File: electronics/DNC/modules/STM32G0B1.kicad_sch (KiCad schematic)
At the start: 1 part

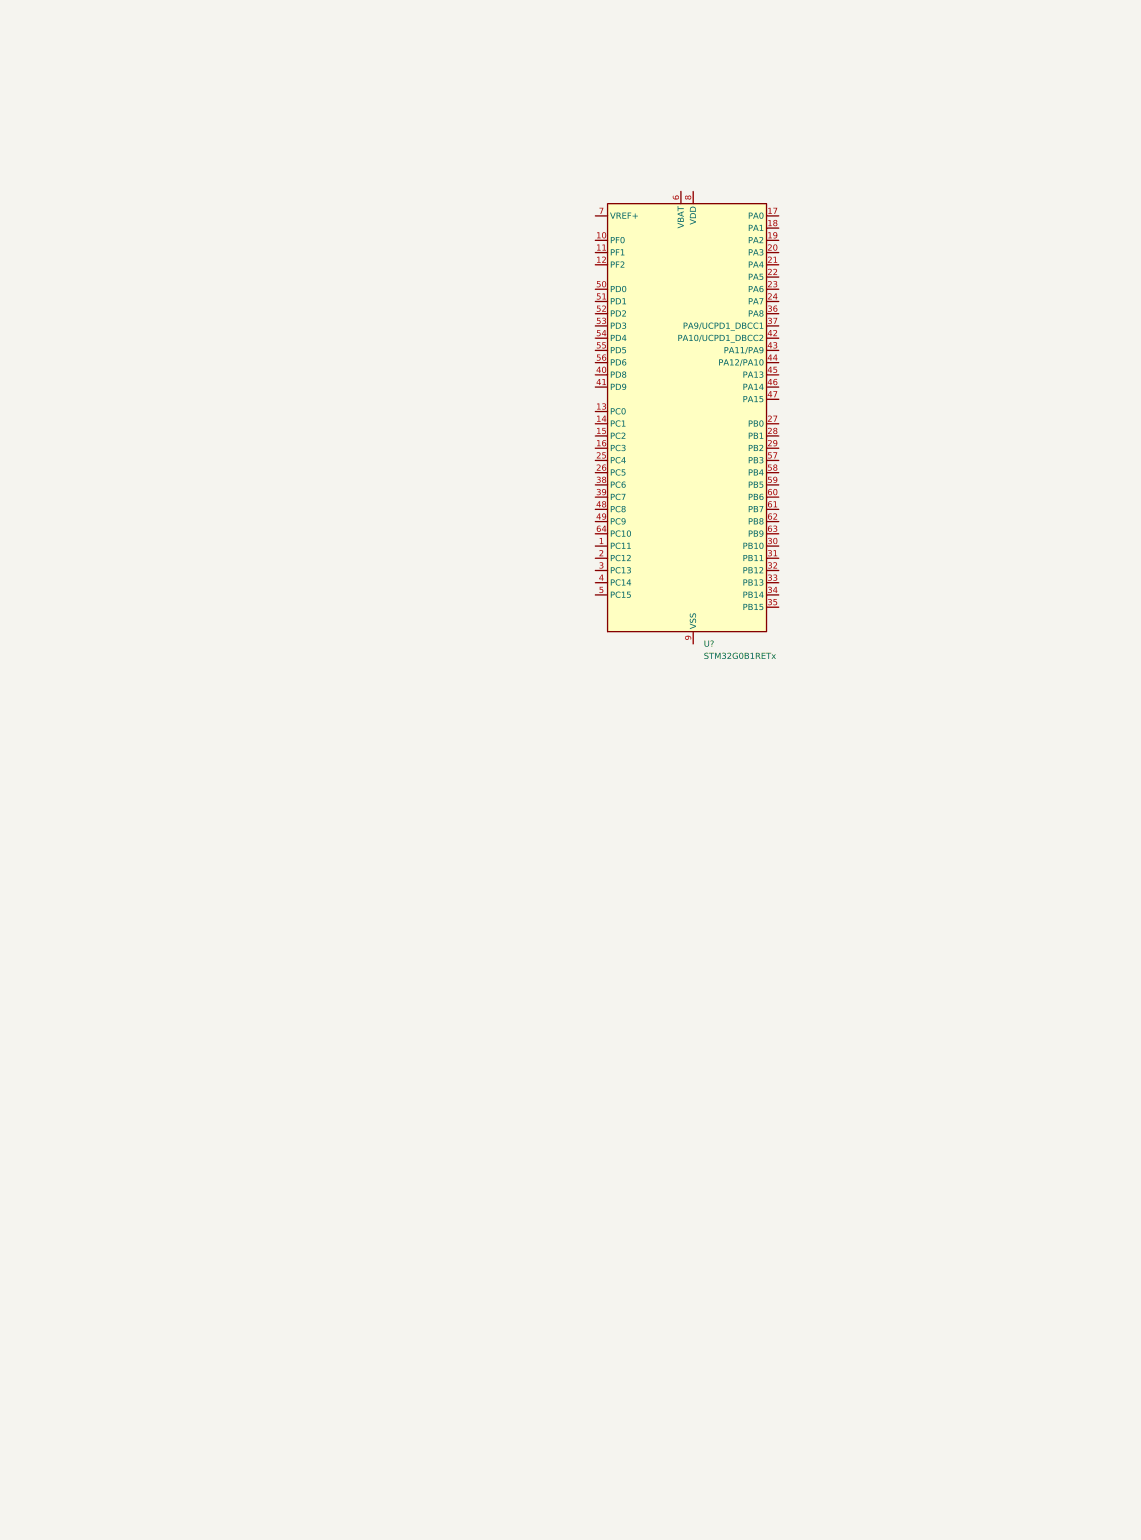
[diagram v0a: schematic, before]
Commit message: Se terminó con el diseño del STM32F4, el PMS, el ESC, el USB-TypeC y el IMU, queda pendiente que la hoja del IMU se cambie por una de sensores.
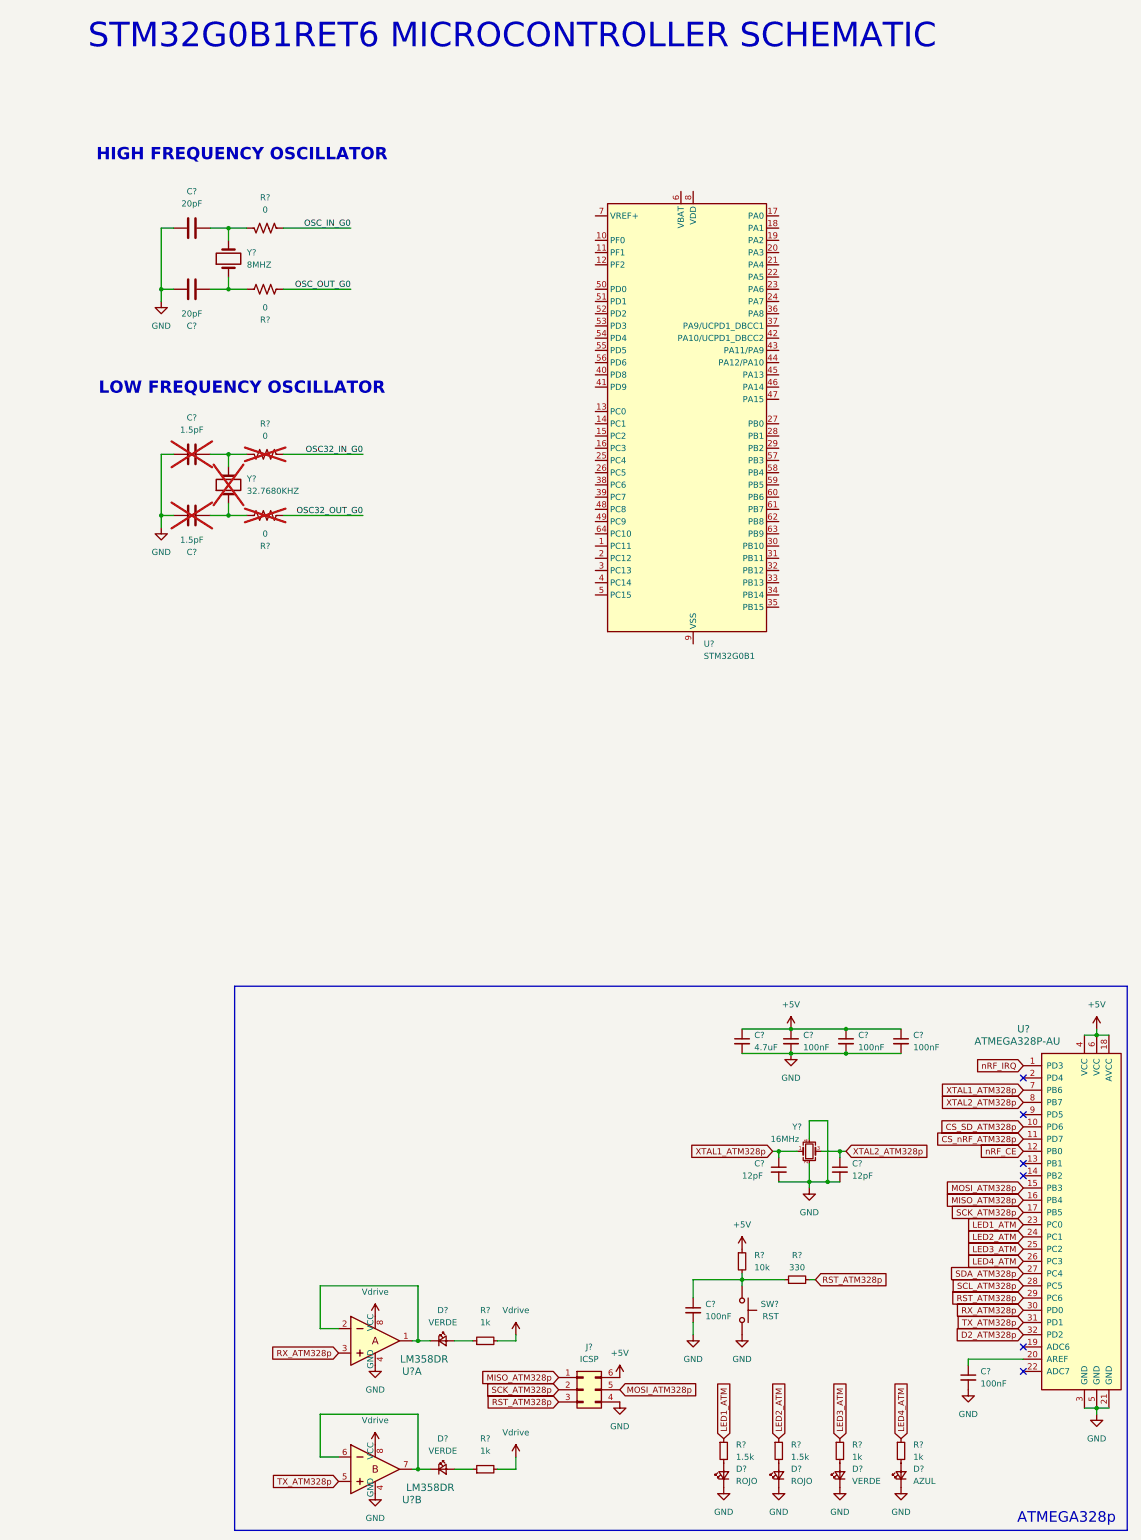
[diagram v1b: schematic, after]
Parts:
- added C? (x5): 100nF, Capacitor_SMD:C_0402_1005Metric, symbol Device:C_Small
- added C? (x2): 20pF, symbol Device:C
- added C? (x2): 12pF, Capacitor_SMD:C_0402_1005Metric, symbol Device:C_Small
- added C? (x2): 1.5pF, symbol Device:C
- added C?: 4.7uF, Capacitor_SMD:C_0402_1005Metric, symbol Device:C_Small
- added D?: AZUL, LED_SMD:LED_0603_1608Metric, symbol Device:LED_Small
- added D? (x3): VERDE, LED_SMD:LED_0603_1608Metric, symbol Device:LED_Small
- added D? (x2): ROJO, LED_SMD:LED_0603_1608Metric, symbol Device:LED_Small
- added J?: ICSP, Connector_PinHeader_2.54mm:PinHeader_2x03_P2.54mm_Vertical, symbol Connector_Generic:Conn_02x03_Counter_Clockwise
- added R? (x4): 0, symbol Device:R_US
- added R?: 330, Resistor_SMD:R_0402_1005Metric, symbol Device:R_Small
- added R?: 10k, Resistor_SMD:R_0402_1005Metric, symbol Device:R_Small
- added R? (x4): 1k, Resistor_SMD:R_0603_1608Metric, symbol Device:R_Small
- added R? (x2): 1.5k, Resistor_SMD:R_0603_1608Metric, symbol Device:R_Small
- added SW?: RST, Gen_devices:KEY-TH_2P-L6.0-W3.5-P6.50, symbol Switch:SW_Push
- added U? (x2): LM358DR, digikey-footprints:SOIC-8_W3.9mm, symbol dk_Linear-Amplifiers-Instrumentation-OP-Amps-Buffer-Amps:LM358DR
- added U?: ATMEGA328P-AU, digikey-footprints:TQFP-32_7x7mm, symbol dk_Embedded-Microcontrollers:ATMEGA328P-AU
- added Y?: 32.7680KHZ, symbol Device:Crystal
- added Y?: 8MHZ, symbol Device:Crystal
- added Y?: 16MHz, Crystal:Crystal_SMD_3225-4Pin_3.2x2.5mm, symbol Device:Crystal_GND24_Small
- U?: value STM32G0B1RETx -> STM32G0B1; Descrip IC MCU 32BIT 512KB FLASH 64LQFP -> (none)
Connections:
- new net: D?.2 (A), R?.2 (x4)
- new net: C?.1, R?.1, Y?.1 (x2)
- new net: C?.2, R?.1, Y?.2 (x2)
- new net: D?.1 (K), U?.6, U?.7
- new net: D?.2 (A), R?.1 (x2)
- new net: D?.1 (K), U?.1, U?.2
- new net: C?.1, R?.1, R?.2, SW?.1
- new net: C?.1, U?.20 (AREF)
- new net +5V: C?.1, C?.1, C?.1, C?.1, J?.6 (Pin_6), R?.1, U?.18 (AVCC), U?.4 (VCC), U?.6 (VCC)
- new net CS_SD_ATM328p: U?.10 (PD6)
- new net CS_nRF_ATM328p: U?.11 (PD7)
- new net D2_ATM328p: U?.32 (PD2)
- new net GND: C?.1, C?.1, C?.2, C?.2, C?.2, C?.2, C?.2, C?.2, C?.2, C?.2, C?.2, C?.2, D?.1 (K), D?.1 (K), D?.1 (K), D?.1 (K), J?.4 (Pin_4), SW?.2, U?.21 (GND), U?.3 (GND), U?.4 (GND), U?.4 (GND), U?.5 (GND), Y?.2, Y?.4
- new net LED1_ATM: R?.1, U?.23 (PC0)
- new net LED2_ATM: R?.1, U?.24 (PC1)
- new net LED3_ATM: R?.1, U?.25 (PC2)
- new net LED4_ATM: R?.1, U?.26 (PC3)
- new net MISO_ATM328p: J?.1 (Pin_1), U?.16 (PB4)
- new net MOSI_ATM328p: J?.5 (Pin_5), U?.15 (PB3)
- new net OSC32_IN_G0: R?.2
- new net OSC32_OUT_G0: R?.2
- new net OSC_IN_G0: R?.2
- new net OSC_OUT_G0: R?.2
- new net RST_ATM328p: J?.3 (Pin_3), R?.2, U?.29 (PC6)
- new net RX_ATM328p: U?.3, U?.30 (PD0)
- new net SCK_ATM328p: J?.2 (Pin_2), U?.17 (PB5)
- new net SCL_ATM328p: U?.28 (PC5)
- new net SDA_ATM328p: U?.27 (PC4)
- new net TX_ATM328p: U?.31 (PD1), U?.5
- new net Vdrive: R?.2, R?.2, U?.8 (VCC), U?.8 (VCC)
- new net XTAL1_ATM328p: C?.1, U?.7 (PB6), Y?.1
- new net XTAL2_ATM328p: C?.1, U?.8 (PB7), Y?.3
- new net nRF_CE: U?.12 (PB0)
- new net nRF_IRQ: U?.1 (PD3)
- no-connect marks 0 -> 6
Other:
- note added: "ATMEGA328p"
- note added: "HIGH FREQUENCY OSCILLATOR"
- note added: "LOW FREQUENCY OSCILLATOR"
- note added: "STM32G0B1RET6 MICROCONTROLLER SCHEMATIC"
- company: (none) -> ${COMPANY}
- title: (none) -> ${TITLE}
